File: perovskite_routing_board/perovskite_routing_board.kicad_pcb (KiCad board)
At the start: 4 copper layers, 57 x 52.2 mm, 6 parts, among them J1 G125-MH12605M4R, U4 MCP9808_MSOP, U5 MCP9808_MSOP, U6 MCP9808_MSOP

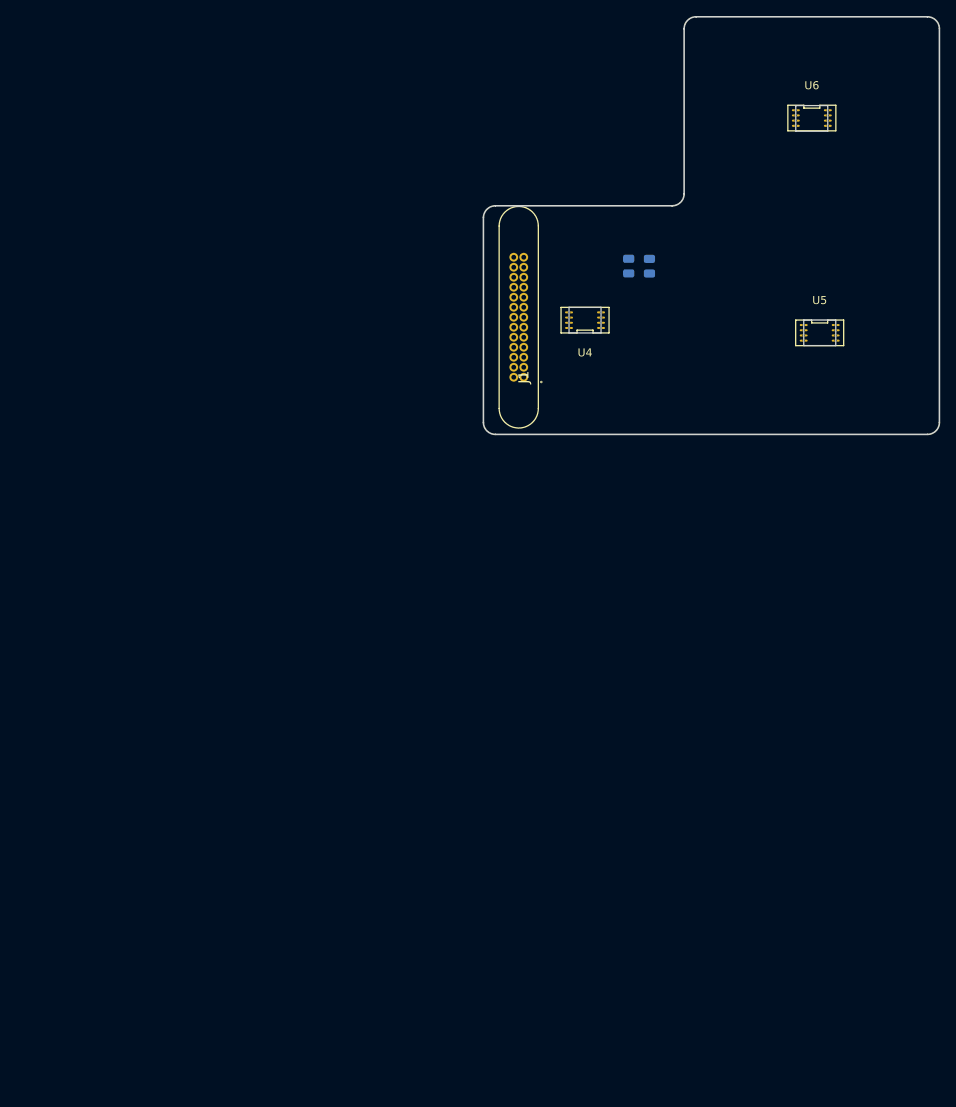
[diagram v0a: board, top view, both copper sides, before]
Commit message: moved headers to fit connection to routing board and switch symbols to proper form
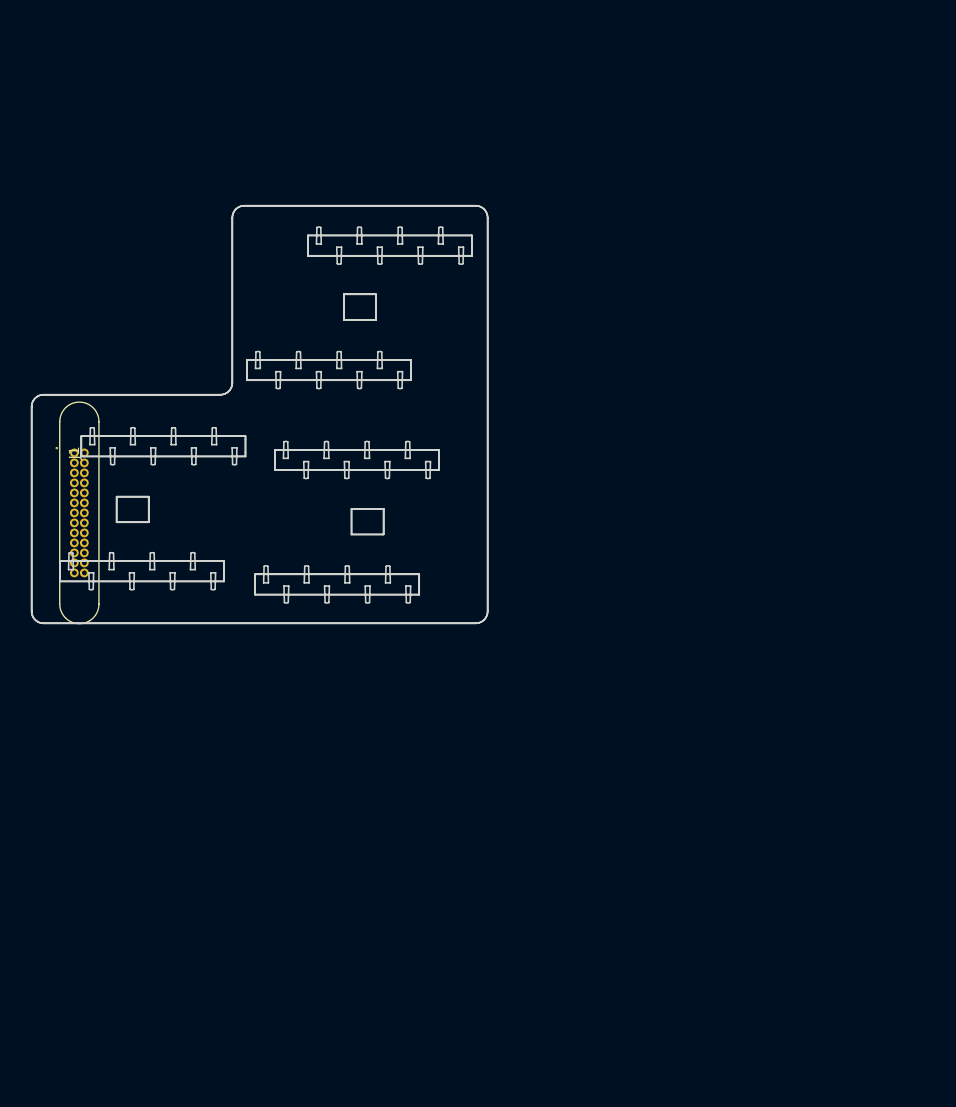
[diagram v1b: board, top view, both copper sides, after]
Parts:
- removed R1, R4: R, Resistor_SMD:R_0805_2012Metric
- removed U4, U5, U6: MCP9808_MSOP, MCP9804Castillated:CastillatedMCP9804
- moved J1 57.0 mm to (120.9, 99.6), turned to 270 degrees
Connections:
- J1 pad 20: SCL -> (no net)
- J1 pad 21: SDA -> (no net)
- J1 pad 22: GND -> (no net)
- J1 pad 23: Vdd -> (no net)
- J1 pad 24: Alert1 -> (no net)
- J1 pad 25: Alert2 -> (no net)
- J1 pad 26: Alert3 -> (no net)
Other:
- outline, holes or cut-outs redrawn

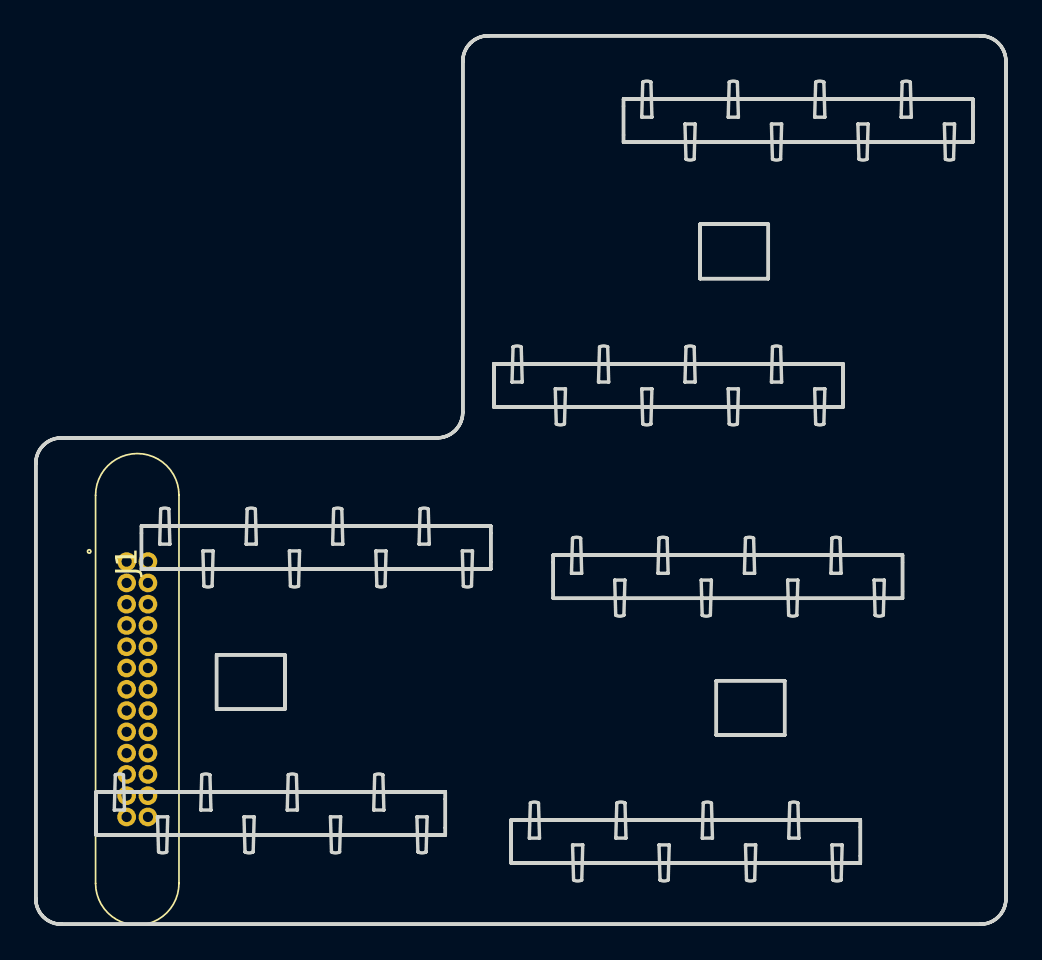
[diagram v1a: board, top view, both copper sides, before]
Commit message: new headers added and spacing fixed to allow for 26 pin connector
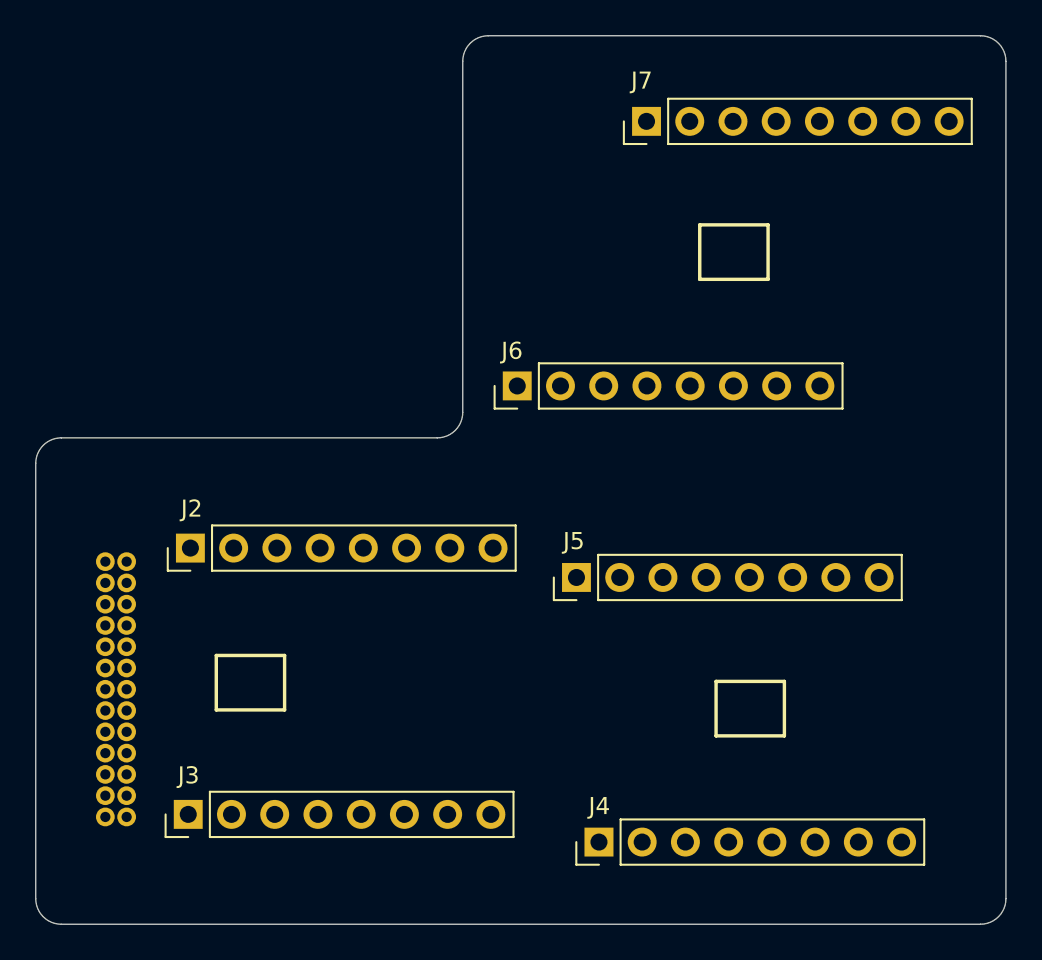
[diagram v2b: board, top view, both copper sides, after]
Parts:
- added J2: Conn_01x08, Connector_PinHeader_2.54mm:PinHeader_1x08_P2.54mm_Vertical, F.Cu at (124.6, 98.8)
- added J3: Conn_01x08, Connector_PinHeader_2.54mm:PinHeader_1x08_P2.54mm_Vertical, F.Cu at (124.5, 114.5)
- added J4: Conn_01x08, Connector_PinHeader_2.54mm:PinHeader_1x08_P2.54mm_Vertical, F.Cu at (148.6, 116.1)
- added J5: Conn_01x08, Connector_PinHeader_2.54mm:PinHeader_1x08_P2.54mm_Vertical, F.Cu at (147.3, 100.6)
- added J6: Conn_01x08, Connector_PinHeader_2.54mm:PinHeader_1x08_P2.54mm_Vertical, F.Cu at (143.8, 89.3)
- added J7: Conn_01x08, Connector_PinHeader_2.54mm:PinHeader_1x08_P2.54mm_Vertical, F.Cu at (151.4, 73.8)
- J1: moved to B.Cu
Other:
- outline, holes or cut-outs redrawn

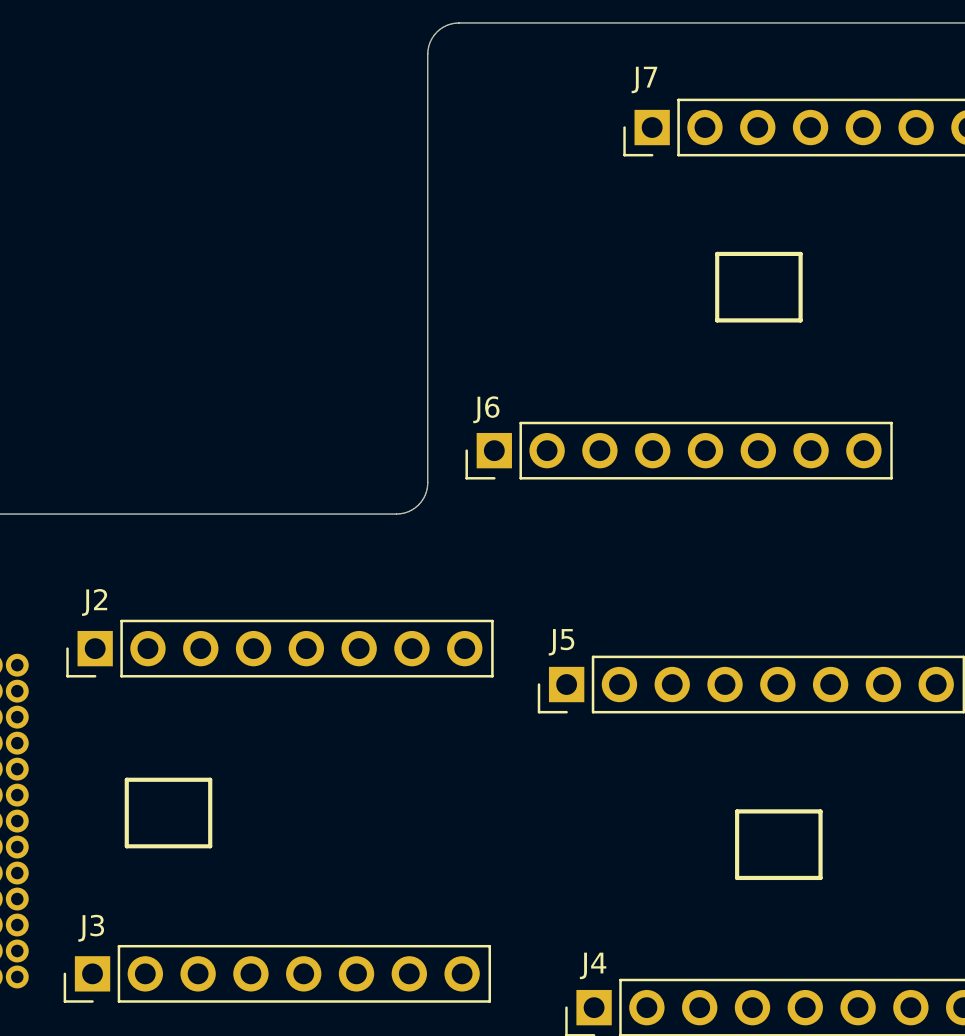
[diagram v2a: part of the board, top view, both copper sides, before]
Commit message: added mounting holes for bottom PCB
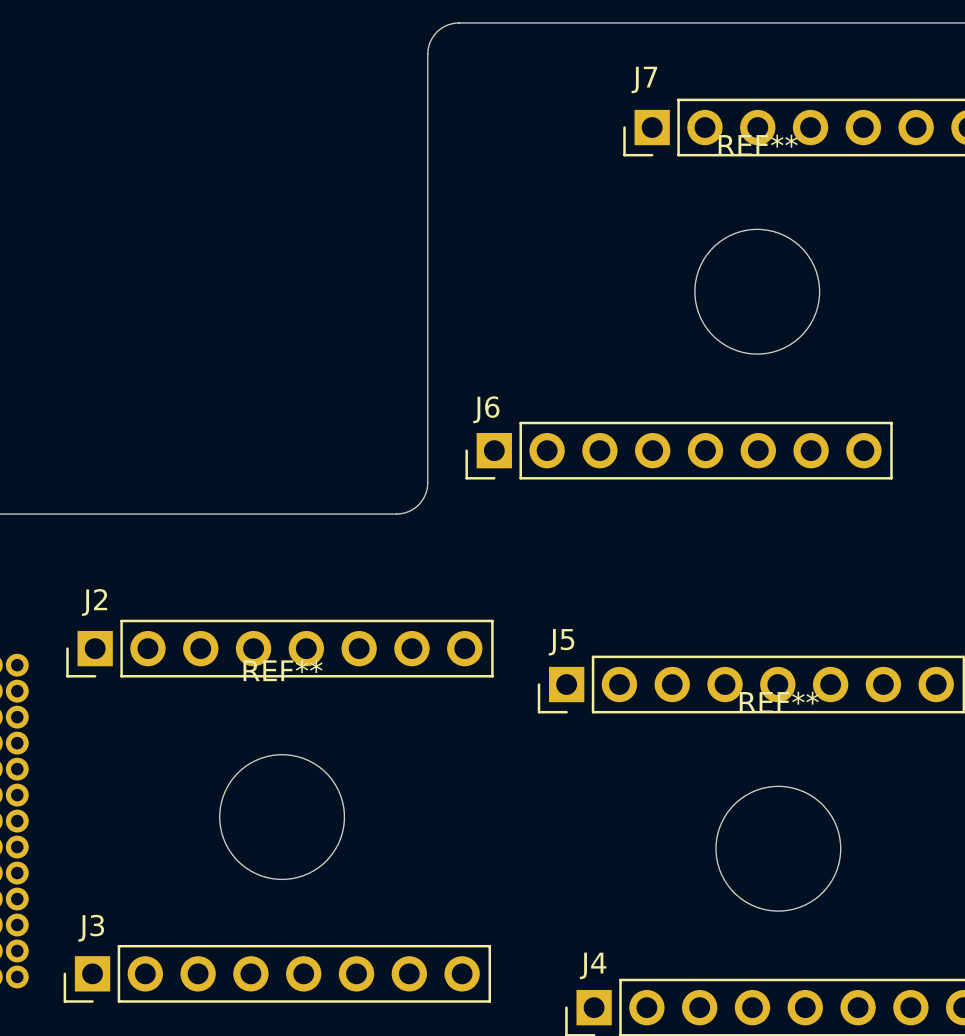
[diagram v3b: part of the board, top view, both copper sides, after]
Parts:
- added REF**: MountingHole_6mm, MountingHole:MountingHole_6mm, F.Cu at (156.5, 81.7)
- added REF**: MountingHole_6mm, MountingHole:MountingHole_6mm, F.Cu at (157.5, 108.5)
- added REF**: MountingHole_6mm, MountingHole:MountingHole_6mm, F.Cu at (133.6, 106.9)

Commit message: update routing board
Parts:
- removed REF** (x3): MountingHole_6mm, MountingHole:MountingHole_6mm
- J1: value G125-MH12605M4R -> Conn_01x08; footprint MV12605M1P:G125-MV12605M1P -> Connector_PinHeader_2.54mm:PinHeader_1x08_P2.54mm_Vertical; moved to F.Cu
- J7: value Conn_01x08 -> G125-MH12605M4R; footprint Connector_PinHeader_2.54mm:PinHeader_1x08_P2.54mm_Vertical -> MV12605M1P:G125-MV12605M1P; moved to B.Cu
- moved J7 80.4 mm to (120.6, 148.0)
- moved J5 76.5 mm to (165.5, 174.9), turned to 270 degrees
- moved J6 69.7 mm to (166.1, 155.3), turned to 270 degrees
- moved J1 51.5 mm to (125.5, 150.9), turned to 90 degrees
- moved J3 44.6 mm to (166.6, 129.1), turned to 270 degrees
- moved J4 37.3 mm to (166.0, 149.0), turned to 270 degrees
- moved J2 30.9 mm to (125.4, 129.8)
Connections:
- J1 pad 1: (no net) -> CP
- J1 pad 2: (no net) -> CELL_6
- J1 pad 3: (no net) -> VDD
- J1 pad 4: (no net) -> CELL_5
- J1 pad 5: (no net) -> SDA
- J1 pad 6: (no net) -> CELL_4
- J1 pad 7: (no net) -> SCL
- J1 pad 8: (no net) -> CP
- J2 pad 1: (no net) -> GND
- J2 pad 2: (no net) -> GND
- J2 pad 3: (no net) -> GND
- J2 pad 4: (no net) -> CELL3
- J2 pad 5: (no net) -> GND
- J2 pad 6: (no net) -> CELL_2
- J2 pad 7: (no net) -> ALERT1
- J2 pad 8: (no net) -> CELL_1
- J3 pad 1: (no net) -> GND
- J3 pad 2: (no net) -> CELL_9
- J3 pad 3: (no net) -> ALERT2
- J3 pad 4: (no net) -> CELL_8
- J3 pad 5: (no net) -> GND
- J3 pad 6: (no net) -> GND
- J3 pad 7: (no net) -> VDD
- J3 pad 8: (no net) -> CELL_7
- J4 pad 1: (no net) -> CP
- J4 pad 2: (no net) -> SCL
- J4 pad 3: (no net) -> CELL_10
- J4 pad 4: (no net) -> SDA
- J4 pad 5: (no net) -> CELL_11
- J4 pad 6: (no net) -> GND
- J4 pad 7: (no net) -> CELL_12
- J4 pad 8: (no net) -> VDD
- J5 pad 1: (no net) -> CELL_16
- J5 pad 2: (no net) -> SCL
- J5 pad 3: (no net) -> GND
- J5 pad 4: (no net) -> SDA
- J5 pad 5: (no net) -> CELL_17
- J5 pad 6: (no net) -> GND
- J5 pad 7: (no net) -> CELL_18
- J5 pad 8: (no net) -> VDD
- J6 pad 1: (no net) -> GND
- J6 pad 2: (no net) -> CELL_15
- J6 pad 3: (no net) -> ALERT3
- J6 pad 4: (no net) -> GND
- J6 pad 5: (no net) -> GND
- J6 pad 6: (no net) -> CELL_14
- J6 pad 7: (no net) -> VDD
- J6 pad 8: (no net) -> CELL_13
- J7 pad 1: (no net) -> Net-(J7-Pad1)
- J7 pad 2: (no net) -> Net-(J7-Pad2)
- J7 pad 3: (no net) -> Net-(J7-Pad3)
- J7 pad 4: (no net) -> Net-(J7-Pad4)
- J7 pad 5: (no net) -> Net-(J7-Pad5)
- J7 pad 6: (no net) -> Net-(J7-Pad6)
- J7 pad 7: (no net) -> Net-(J7-Pad7)
- J7 pad 8: (no net) -> Net-(J7-Pad8)
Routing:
- net SDA: track 0.00 -> 126.7 mm
- net SCL: track 0.00 -> 117.6 mm
- net VDD: track 0.00 -> 105.4 mm
- net CELL_16: track 0.00 -> 77.4 mm
- net CELL_17: track 0.00 -> 60.7 mm
- net CELL_15: track 0.00 -> 55.9 mm
- net CELL_18: track 0.00 -> 55.2 mm
- net ALERT3: track 0.00 -> 54.0 mm
- net CP: track 0.00 -> 49.8 mm
- net CELL_9: track 0.00 -> 44.6 mm
- net ALERT2: track 0.00 -> 44.4 mm
- net CELL_10: track 0.00 -> 43.6 mm
- net CELL_8: track 0.00 -> 43.3 mm
- net CELL_11: track 0.00 -> 37.2 mm
- net CELL_1: track 0.00 -> 37.0 mm
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- added copper zone on B.Cu, net GND
- added copper zone on F.Cu, net GND
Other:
- outline, holes or cut-outs redrawn
- copper layers 4 -> 2
- net class Default: clearance 0.2 -> 0.1524; trace_width 0.25 -> 0.1524
- rule pad_to_mask_clearance: 0 -> 0.0508
- rule trace_clearance: 0.2 -> 0.1524
- rule trace_min: 0.2 -> 0.1524
- rule via_min_drill: 0.3 -> 0.254
- rule via_min_size: 0.4 -> 0.508
